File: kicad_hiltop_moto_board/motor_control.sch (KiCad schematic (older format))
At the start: 48 parts, among them Q1 CSD18540Q5B, Q2 CSD18540Q5B, Q3 CSD18540Q5B, Q4 CSD18540Q5B, Q5 CSD18540Q5B, Q6 CSD18540Q5B, Q7 CSD18540Q5B, Q8 CSD18540Q5B, U1 DRV8704

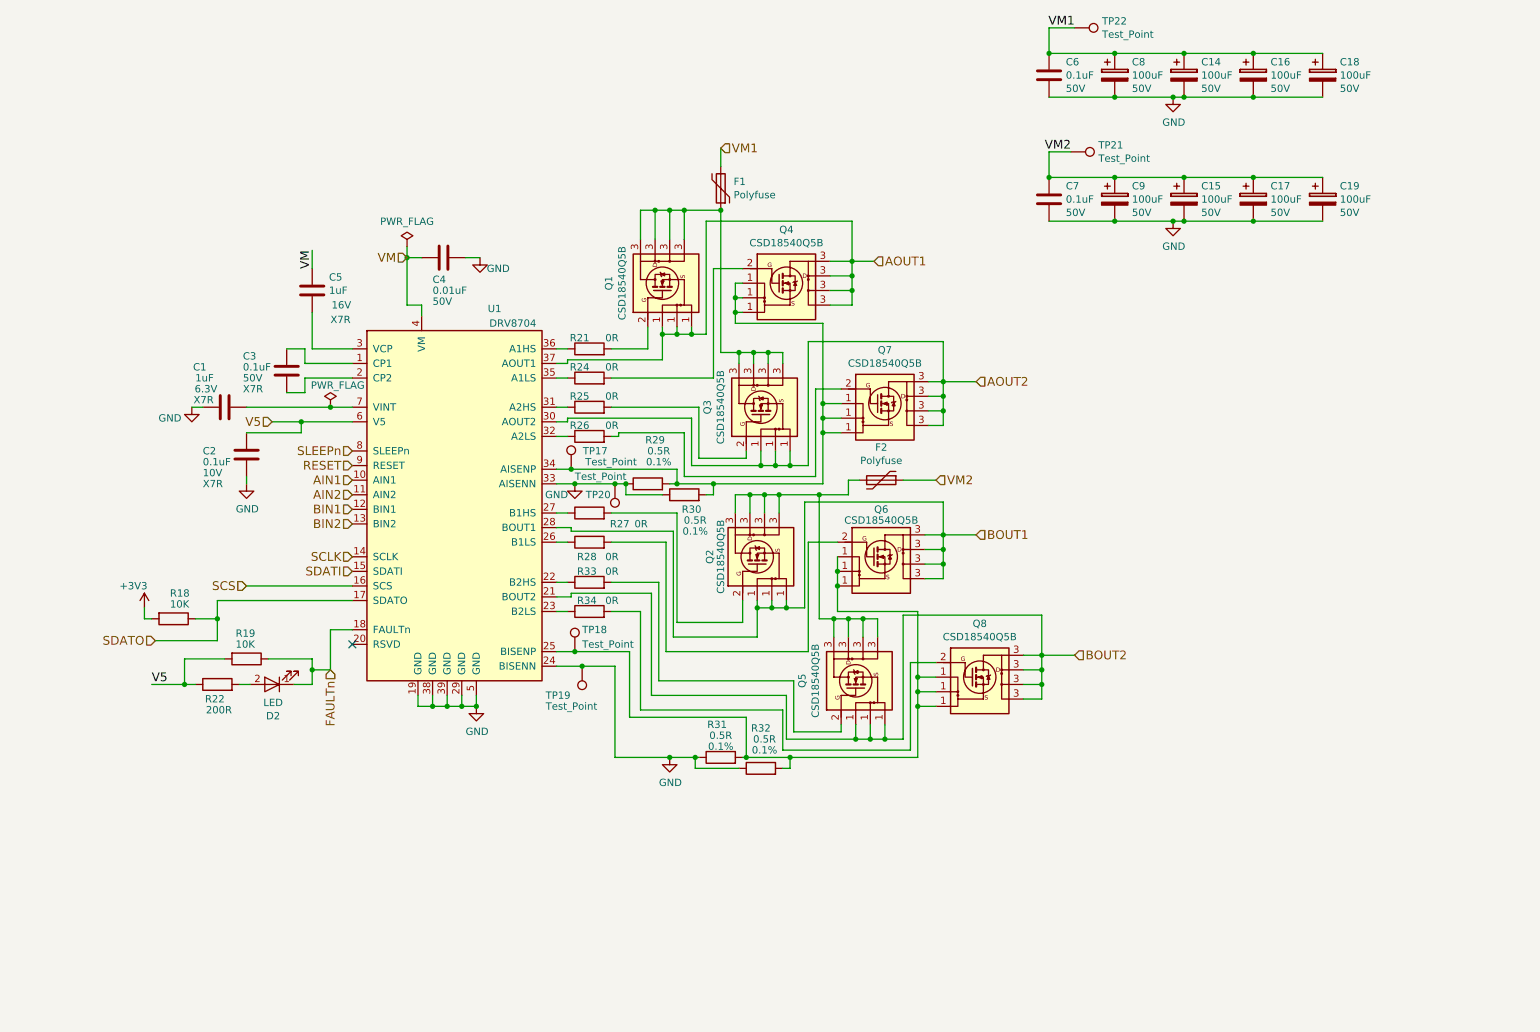
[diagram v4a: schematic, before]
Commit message: Moto vboard test points added
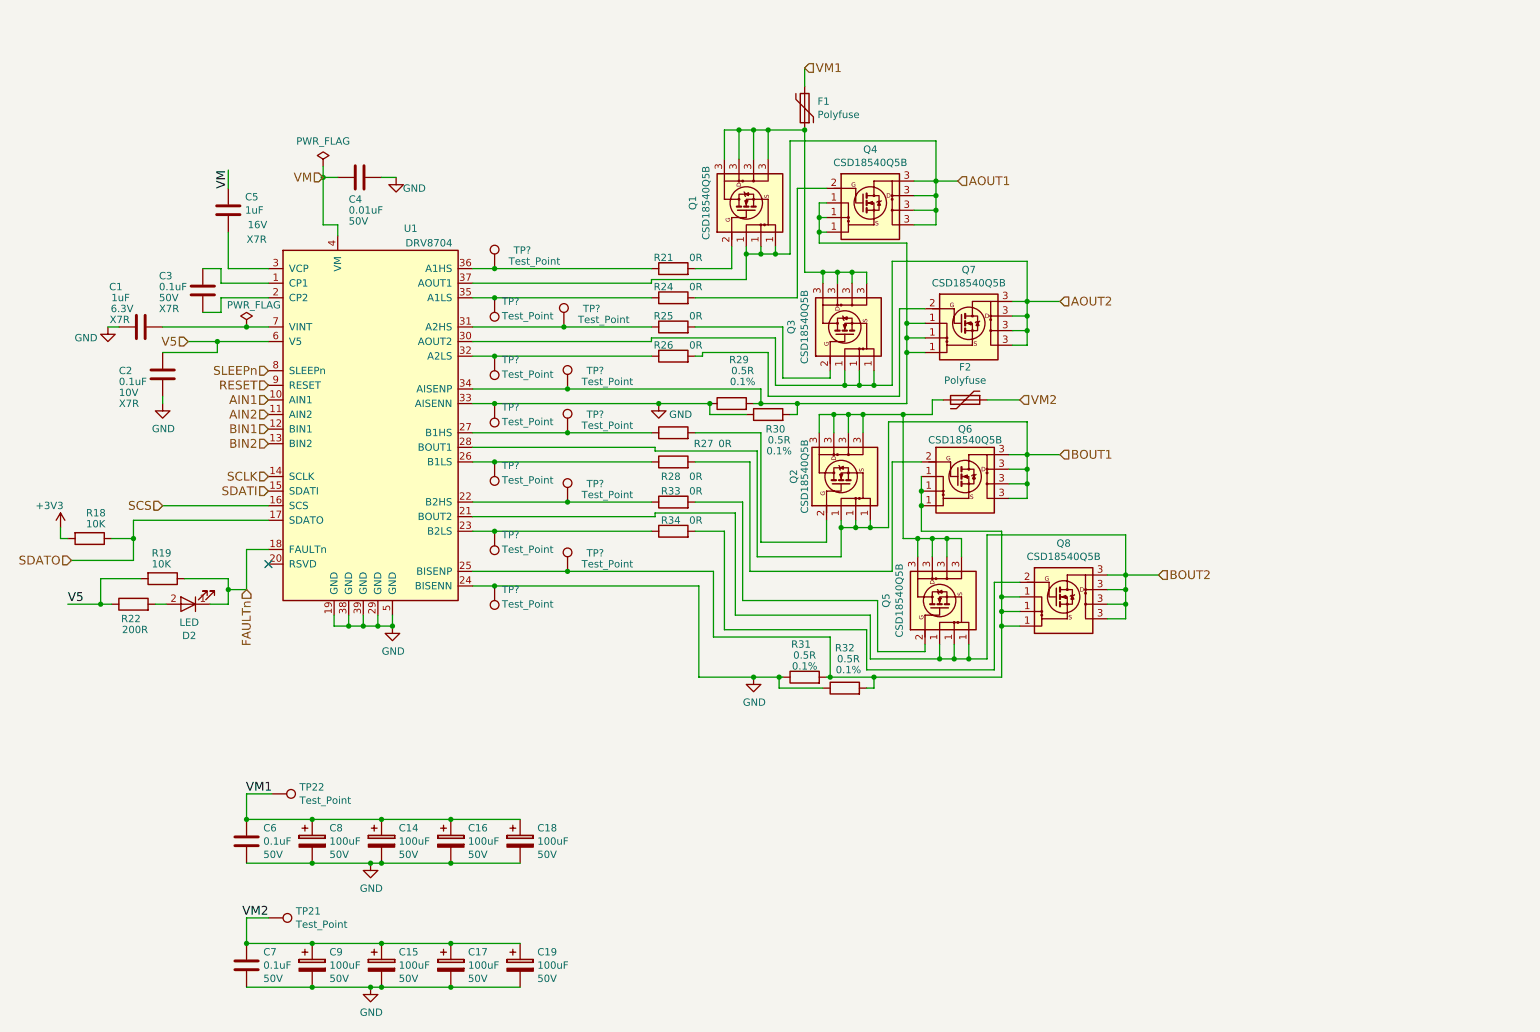
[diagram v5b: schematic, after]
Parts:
- removed TP17, TP18, TP19, TP20: Test_Point, TestPoint:TestPoint_THTPad_D1.0mm_Drill0.5mm, symbol Connector:Test_Point
- added TP? (x12): Test_Point, TestPoint:TestPoint_THTPad_D1.0mm_Drill0.5mm, symbol Connector:Test_Point
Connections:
- net GND: now also TP?.1, TP?.1
- net at Q6.1 (S), Q8.1 (S), R31.2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: now also TP?.1
- net at Q4.1 (S), Q7.1 (S), R29.2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: now also TP?.1
- net at R24.1, U1.35 (A1LS): now also TP?.1
- net at R25.1, U1.31 (A2HS): now also TP?.1
- net at R26.1, U1.32 (A2LS): now also TP?.1
- net at R27.1, U1.27 (B1HS): now also TP?.1
- net at R28.1, U1.26 (B1LS): now also TP?.1
- net at R33.1, U1.22 (B2HS): now also TP?.1
- net at R34.1, U1.23 (B2LS): now also TP?.1
- net at R21.1, U1.36 (A1HS): now also TP?.1
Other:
- moved on the sheet: C1, C14, C15, C16, C17, C18, C19, C2, C3, C4, C5, C6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

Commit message: Moto board awaiting review
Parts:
- added D5: GRN, LED_SMD:LED_0603_1608Metric, symbol device:LED
- added R23, R47: 10K, Resistor_SMD:R_0603_1608Metric, symbol device:R
- added R48: DNF, Resistor_SMD:R_0603_1608Metric, symbol device:R
- D2: value LED -> RED
- R29, R30, R31, R32: value 0.5R -> 0.015R
- gave numbers to parts that had none: 12
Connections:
- net VM1 is gone; now on net VM: C14.1, C16.1, C18.1, C6.1, C8.1, F1.2, TP22.1
- net VM2 is gone; now on net VM: C15.1, C17.1, C19.1, C7.1, C9.1, F2.1, TP21.1
- net GND: now also D5.1 (K), R48.1
- net SLEEPn: now also R47.2, R48.2
- net V5: now also R23.1, R47.1
- new net: D5.2 (A), R23.2
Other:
- note added: "Internal regulator status\n"
- note added: "Motor A Capacitors"
- note added: "Motor B Capacitors"
- moved on the sheet: C1, C2, C3, C4, C5, D2, F1, F2, Q1, Q2, Q3, Q4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

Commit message: Moto board connectors moved
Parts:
- C1, C5: footprint Capacitor_SMD:C_0402_1005Metric -> Capacitor_SMD:C_0603_1608Metric
- F1, F2: footprint Fuse:Fuse_2920_7451Metric -> Fuse:Fuse_Bourns_MF-RHT200
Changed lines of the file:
@@
 F 0 "C5" H 4265 2116 50  0000 L CNN
 F 1 "1uF" H 4265 2025 50  0000 L CNN
-F 2 "Capacitor_SMD:C_0402_1005Metric" H 4188 1875 50  0001 C CNN
+F 2 "Capacitor_SMD:C_0603_1608Metric" H 4188 1875 50  0001 C CNN
 F 3 "" H 4150 2025 50  0001 C CNN
 F 4 "16V" H 4350 1925 50  0000 C CNN "Voltage"
@@
 F 0 "C1" V 3825 2950 50  0000 L CNN
 F 1 "1uF" V 3750 2900 50  0000 L CNN
-F 2 "Capacitor_SMD:C_0402_1005Metric" H 3588 2675 50  0001 C CNN
+F 2 "Capacitor_SMD:C_0603_1608Metric" H 3588 2675 50  0001 C CNN
 F 3 "" H 3550 2825 50  0001 C CNN
 F 4 "6.3V" V 3675 2875 50  0000 L CNN "Voltage"
@@
 F 0 "F1" H 8012 1279 50  0000 R CNN
 F 1 "Polyfuse" H 8012 1370 50  0000 R CNN
-F 2 "Fuse:Fuse_2920_7451Metric" H 8150 1125 50  0001 L CNN
+F 2 "Fuse:Fuse_Bourns_MF-RHT200" H 8150 1125 50  0001 L CNN
 F 3 "" H 8100 1325 50  0001 C CNN
 	1    8100 1325
@@
 F 0 "F2" V 8975 3325 50  0000 C CNN
 F 1 "Polyfuse" V 9066 3325 50  0000 C CNN
-F 2 "Fuse:Fuse_2920_7451Metric" H 9250 3125 50  0001 L CNN
+F 2 "Fuse:Fuse_Bourns_MF-RHT200" H 9250 3125 50  0001 L CNN
 F 3 "" H 9200 3325 50  0001 C CNN
 	1    9200 3325

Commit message: Moto board csd mosfet footprint changes
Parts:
- Q1, Q2, Q3, Q4, Q5, Q6, Q7, Q8: footprint Devtank_PCB_Lib:CSD18540Q5B -> Devtank_PCB_Lib:TI_CSD18540Q5B
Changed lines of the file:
@@
 F 0 "Q1" H 7750 2392 50  0000 C CNN
 F 1 "CSD18540Q5B" H 7750 2301 50  0000 C CNN
-F 2 "Devtank_PCB_Lib:CSD18540Q5B" H 7750 2025 50  0001 C CIN
+F 2 "Devtank_PCB_Lib:TI_CSD18540Q5B" H 7750 2025 50  0001 C CIN
 F 3 "http://www.ti.com/lit/gpn/csd18540q5b" H 7700 2025 50  0001 L CNN
 	1    7750 1975
@@
 F 0 "Q4" H 8550 2442 50  0000 C CNN
 F 1 "CSD18540Q5B" H 8550 2351 50  0000 C CNN
-F 2 "Devtank_PCB_Lib:CSD18540Q5B" H 8550 2075 50  0001 C CIN
+F 2 "Devtank_PCB_Lib:TI_CSD18540Q5B" H 8550 2075 50  0001 C CIN
 F 3 "http://www.ti.com/lit/gpn/csd18540q5b" H 8500 2075 50  0001 L CNN
 	1    8550 2025
@@
 F 0 "Q3" H 8425 3242 50  0000 C CNN
 F 1 "CSD18540Q5B" H 8425 3151 50  0000 C CNN
-F 2 "Devtank_PCB_Lib:CSD18540Q5B" H 8425 2875 50  0001 C CIN
+F 2 "Devtank_PCB_Lib:TI_CSD18540Q5B" H 8425 2875 50  0001 C CIN
 F 3 "http://www.ti.com/lit/gpn/csd18540q5b" H 8375 2875 50  0001 L CNN
 	1    8425 2825
@@
 F 0 "Q7" H 9225 3267 50  0000 C CNN
 F 1 "CSD18540Q5B" H 9225 3176 50  0000 C CNN
-F 2 "Devtank_PCB_Lib:CSD18540Q5B" H 9225 2900 50  0001 C CIN
+F 2 "Devtank_PCB_Lib:TI_CSD18540Q5B" H 9225 2900 50  0001 C CIN
 F 3 "http://www.ti.com/lit/gpn/csd18540q5b" H 9175 2900 50  0001 L CNN
 	1    9225 2850
@@
 F 0 "Q2" H 8400 4225 50  0000 C CNN
 F 1 "CSD18540Q5B" H 8325 4150 50  0000 C CNN
-F 2 "Devtank_PCB_Lib:CSD18540Q5B" H 8400 3900 50  0001 C CIN
+F 2 "Devtank_PCB_Lib:TI_CSD18540Q5B" H 8400 3900 50  0001 C CIN
 F 3 "http://www.ti.com/lit/gpn/csd18540q5b" H 8350 3900 50  0001 L CNN
 	1    8400 3850
@@
 F 0 "Q6" H 9200 4275 50  0000 C CNN
 F 1 "CSD18540Q5B" H 9200 4200 50  0000 C CNN
-F 2 "Devtank_PCB_Lib:CSD18540Q5B" H 9200 3950 50  0001 C CIN
+F 2 "Devtank_PCB_Lib:TI_CSD18540Q5B" H 9200 3950 50  0001 C CIN
 F 3 "http://www.ti.com/lit/gpn/csd18540q5b" H 9150 3950 50  0001 L CNN
 	1    9200 3900
@@
 F 0 "Q5" H 9075 5117 50  0000 C CNN
 F 1 "CSD18540Q5B" H 9075 5026 50  0000 C CNN
-F 2 "Devtank_PCB_Lib:CSD18540Q5B" H 9075 4750 50  0001 C CIN
+F 2 "Devtank_PCB_Lib:TI_CSD18540Q5B" H 9075 4750 50  0001 C CIN
 F 3 "http://www.ti.com/lit/gpn/csd18540q5b" H 9025 4750 50  0001 L CNN
 	1    9075 4700
@@
 F 0 "Q8" H 9875 5142 50  0000 C CNN
 F 1 "CSD18540Q5B" H 9875 5051 50  0000 C CNN
-F 2 "Devtank_PCB_Lib:CSD18540Q5B" H 9875 4775 50  0001 C CIN
+F 2 "Devtank_PCB_Lib:TI_CSD18540Q5B" H 9875 4775 50  0001 C CIN
 F 3 "http://www.ti.com/lit/gpn/csd18540q5b" H 9825 4775 50  0001 L CNN
 	1    9875 4725
